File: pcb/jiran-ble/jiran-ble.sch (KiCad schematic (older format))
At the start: 166 parts, among them J1 BATT, J2 USB-C Conn, J3 SWD, J4 BATT, J5 USB-C Conn, J6 SWD, Q1 AO3407, Q3 AO3407, SW1 SW_PUSH, SW10 SW_Push, SW11 SW_Push, SW12 SW_Push, SW13 SW_Push, SW14 SW_Push, SW15 SW_Push, SW16 SW_Push, SW17 SW_Push, SW18 SW_Push, SW19 SW_Push, SW2 SW_Push, SW20 SW_Push, SW21 SW_Push, SW22 SW_Push, SW23 SW_Push, SW24 SW_Push, SW25 SW_Push, SW26 SW_Push, SW27 SW_Push, SW28 SW_Push, SW29 SW_Push, SW3 SW_Push, SW30 SW_PUSH, SW31 SW_Push, SW32 SW_Push, SW33 SW_Push, SW34 SW_Push, SW35 SW_Push, SW36 SW_Push, SW37 SW_Push, SW38 SW_Push, SW39 SW_Push, SW4 SW_Push, SW40 SW_Push, SW41 SW_Push, SW42 SW_Push, SW43 SW_Push, SW44 SW_Push, SW45 SW_Push, SW46 SW_Push, SW47 SW_Push, SW48 SW_Push, SW49 SW_Push, SW5 SW_Push, SW50 SW_Push, SW51 SW_Push, SW52 SW_Push, SW53 SW_Push, SW54 SW_Push, SW55 SW_Push, SW56 SW_Push, SW57 SW_Push, SW58 SW_Push, SW6 SW_Push, SW7 SW_Push, SW8 SW_Push, SW9 SW_Push, U1 XC6220B331MR-G, U2 E73-2G4M08S1C, U3 TP4054, U4 XC6220B331MR-G, U5 E73-2G4M08S1C, U6 TP4054, X1 Crystal, X2 Crystal

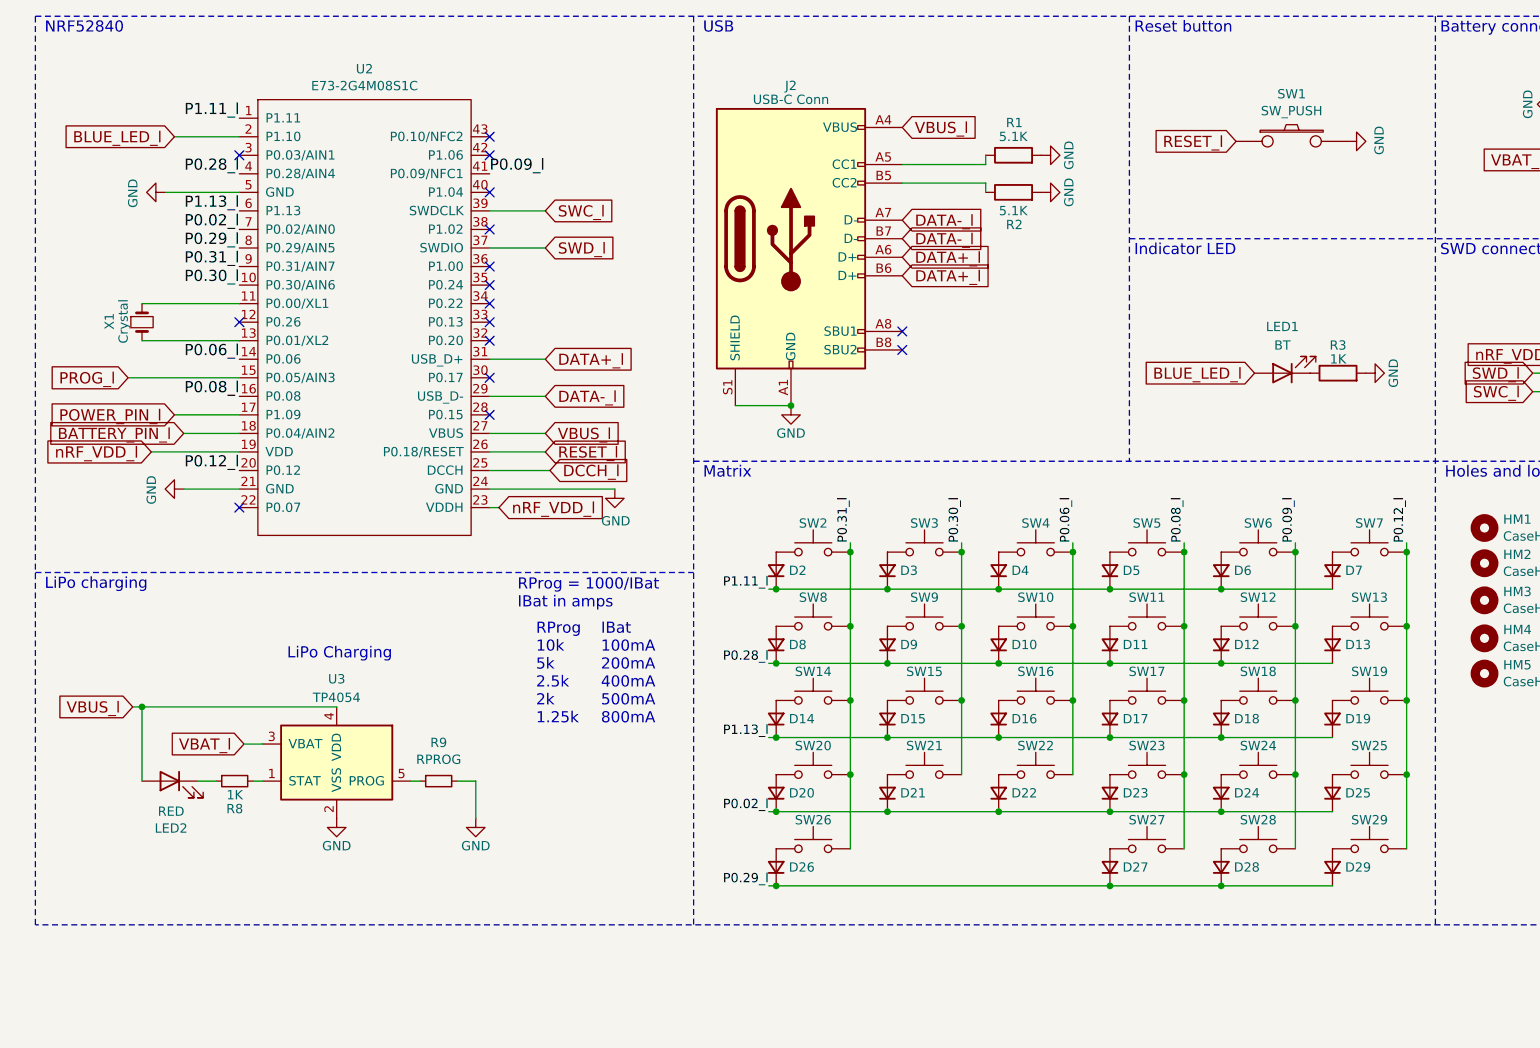
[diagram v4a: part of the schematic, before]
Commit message: Change controller module
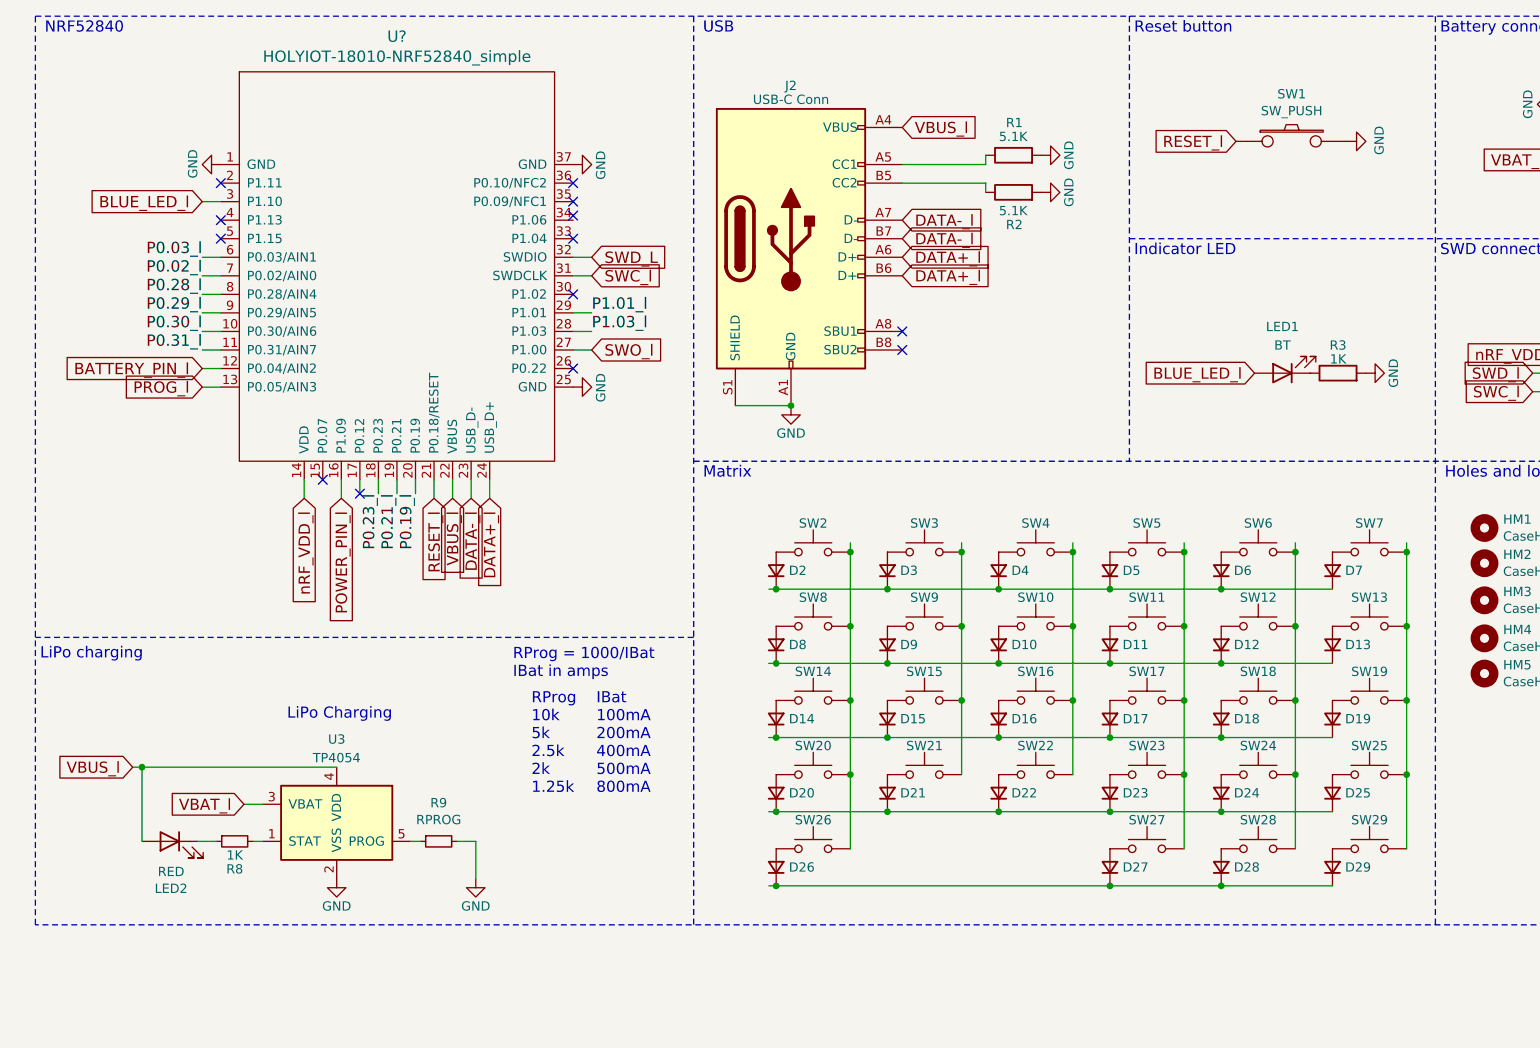
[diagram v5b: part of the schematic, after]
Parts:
- removed U2: E73-2G4M08S1C, jiran-ble:E73-2G4M08S1C-52840, symbol candy-rescue:E73-2G4M08S1C-52840-nrfmicro
- removed X1: Crystal, jiran-ble:Crystal_SMD_CM9V, symbol Device:Crystal_Small
- added U?: HOLYIOT-18010-NRF52840_simple, symbol jiran-ble:HOLYIOT-18010-NRF52840_simple
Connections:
- net labels added: P0.03_l, P0.19_l, P0.21_l, P0.23_l, P1.01_l, P1.03_l, SWD_L, SWO_l
- net labels removed: DCCH_l, P0.06_l, P0.08_l, P0.09_l, P0.12_l, P1.11_l, P1.13_l
- wire segments 227 -> 233
- no-connect marks 33 -> 30
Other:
- moved on the sheet: LED2, R8, R9, U3

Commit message: USB circuit is now simpler
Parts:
- removed R1, R2: 5.1K, jiran-ble:Resistor_SMD_0805, symbol Device:R
- added R? (x2): 5.1k, symbol Device:R_Small
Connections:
- net labels added: D+_l, D-_l
- wire segments 233 -> 245
- no-connect marks 30 -> 31
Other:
- note added: "USB-C"
- moved on the sheet: J2
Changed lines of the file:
@@
 NRF52840
 Text Notes 4100 600  0    60   ~ 0
-USB
+USB-C
 Text Notes 6425 1800 0    60   ~ 0
 Indicator LED
@@
 Text Notes 15415 11075 0    70   ~ 14
 r0.2
-Text GLabel 5175 1600 2    60   Input ~ 0
-DATA-_l
-$Comp
-L Device:R R2
-U 1 1 5CAA680B
-P 5775 1450
-F 0 "R2" V 5600 1400 50  0000 L CNN
-F 1 "5.1K" V 5675 1375 50  0000 L CNN
-F 2 "jiran-ble:Resistor_SMD_0805" V 5705 1450 50  0001 C CNN
-F 3 "~" H 5775 1450 50  0001 C CNN
-	1    5775 1450
-	0    -1   -1   0
-$EndComp
-$Comp
-L Device:R R1
-U 1 1 5CAA879F
-P 5775 1250
-F 0 "R1" V 5950 1200 50  0000 L CNN
-F 1 "5.1K" V 5875 1175 50  0000 L CNN
-F 2 "jiran-ble:Resistor_SMD_0805" V 5705 1250 50  0001 C CNN
-F 3 "~" H 5775 1250 50  0001 C CNN
-	1    5775 1250
-	0    -1   -1   0
-$EndComp
-Text GLabel 5175 1700 2    60   Input ~ 0
-DATA-_l
-Text GLabel 5175 1800 2    60   Input ~ 0
-DATA+_l
-Text GLabel 5175 1900 2    60   Input ~ 0
-DATA+_l
 $Comp
 L power:GND #PWR04
 U 1 1 5E5DBB46
-P 5925 1250
-F 0 "#PWR04" H 5925 1000 50  0001 C CNN
-F 1 "GND" H 5925 1100 50  0000 C CNN
-F 2 "" H 5925 1250 50  0001 C CNN
-F 3 "" H 5925 1250 50  0001 C CNN
-	1    5925 1250
-	0    -1   -1   0
-$EndComp
-$Comp
-L power:GND #PWR06
-U 1 1 5E5DDBCF
-P 5925 1450
-F 0 "#PWR06" H 5925 1200 50  0001 C CNN
-F 1 "GND" H 5925 1300 50  0000 C CNN
-F 2 "" H 5925 1450 50  0001 C CNN
-F 3 "" H 5925 1450 50  0001 C CNN
-	1    5925 1450
+P 6050 1300
+F 0 "#PWR04" H 6050 1050 50  0001 C CNN
+F 1 "GND" H 6050 1150 50  0000 C CNN
+F 2 "" H 6050 1300 50  0001 C CNN
+F 3 "" H 6050 1300 50  0001 C CNN
+	1    6050 1300
 	0    -1   -1   0
 $EndComp
@@
 L power:GND #PWR013
 U 1 1 5E5EC00A
-P 4575 2600
-F 0 "#PWR013" H 4575 2350 50  0001 C CNN
-F 1 "GND" H 4575 2450 50  0000 C CNN
-F 2 "" H 4575 2600 50  0001 C CNN
-F 3 "" H 4575 2600 50  0001 C CNN
-	1    4575 2600
+P 4650 2550
+F 0 "#PWR013" H 4650 2300 50  0001 C CNN
+F 1 "GND" H 4650 2400 50  0000 C CNN
+F 2 "" H 4650 2550 50  0001 C CNN
+F 3 "" H 4650 2550 50  0001 C CNN
+	1    4650 2550
 	1    0    0    -1
 $EndComp
-Text GLabel 5175 1100 2    60   Input ~ 0
+Text GLabel 5350 1050 2    60   Input ~ 0
 VBUS_l
 $Comp
 L nrfmicro-rescue:USB_C_Receptacle_USB2.0-Connector J2
 U 1 1 5C743564
-P 4575 1700
-F 0 "J2" H 4575 2525 50  0000 C CNN
-F 1 "USB-C Conn" H 4575 2450 50  0000 C CNN
-F 2 "jiran-ble:USB-C_MidMount" H 4682 2475 50  0001 C CNN
-F 3 "https://www.usb.org/sites/default/files/documents/usb_type-c.zip" H 4725 1700 50  0001 C CNN
-	1    4575 1700
+P 4650 1650
+F 0 "J2" H 4650 2475 50  0000 C CNN
+F 1 "USB-C Conn" H 4650 2400 50  0000 C CNN
+F 2 "jiran-ble:USB-C_MidMount" H 4757 2425 50  0001 C CNN
+F 3 "https://www.usb.org/sites/default/files/documents/usb_type-c.zip" H 4800 1650 50  0001 C CNN
+	1    4650 1650
 	1    0    0    -1
 $EndComp
@@
 Connection ~ 1075 4550
 Wire Wire Line
-	4275 2600 4575 2600
-Connection ~ 4575 2600
-Wire Wire Line
 	1675 4950 1725 4950
 Wire Wire Line
@@
 Wire Wire Line
 	11825 2050 11925 2050
-NoConn ~ 5175 2200
-NoConn ~ 5175 2300
+NoConn ~ 5250 2150
+NoConn ~ 5250 2250
 Text Notes 3175 4700 0    60   ~ 0
 RProg\n10k\n5k\n2.5k\n2k\n1.25k
@@
 Text Notes 3075 4075 0    60   ~ 0
 RProg = 1000/IBat\nIBat in amps
-Wire Wire Line
-	5175 1300 5625 1300
-Wire Wire Line
-	5625 1300 5625 1250
-Wire Wire Line
-	5175 1400 5625 1400
-Wire Wire Line
-	5625 1400 5625 1450
 Text GLabel 8775 2325 0    60   Input ~ 0
 nRF_VDD_l
@@
 NoConn ~ 3400 2000
 NoConn ~ 3400 1700
-NoConn ~ 3400 1575
+NoConn ~ 3400 1600
 NoConn ~ 3400 1500
 NoConn ~ 3400 1400
 NoConn ~ 1500 1600
 NoConn ~ 1500 1700
+$Comp
+L Device:R_Small R?
+U 1 1 609F1795
+P 5850 1250
+F 0 "R?" V 6025 1250 50  0000 C CNN
+F 1 "5.1k" V 5925 1250 50  0000 C CNN
+F 2 "" H 5850 1250 50  0001 C CNN
+F 3 "~" H 5850 1250 50  0001 C CNN
+	1    5850 1250
+	0    -1   -1   0
+$EndComp
+$Comp
+L Device:R_Small R?
+U 1 1 609F2B00
+P 5850 1350
+F 0 "R?" V 6025 1350 50  0000 C CNN
+F 1 "5.1k" V 5925 1350 50  0000 C CNN
+F 2 "" H 5850 1350 50  0001 C CNN
+F 3 "~" H 5850 1350 50  0001 C CNN
+	1    5850 1350
+	0    1    1    0
+$EndComp
+Text GLabel 5450 1600 2    61   Input ~ 0
+D-_l
+Wire Wire Line
+	5250 1550 5350 1550
+Wire Wire Line
+	5350 1650 5250 1650
+Wire Wire Line
+	5350 1550 5350 1600
+Wire Wire Line
+	5450 1600 5350 1600
+Connection ~ 5350 1600
+Wire Wire Line
+	5350 1600 5350 1650
+Text GLabel 5450 1800 2    61   Input ~ 0
+D+_l
+Wire Wire Line
+	5250 1750 5350 1750
+Wire Wire Line
+	5350 1850 5250 1850
+Wire Wire Line
+	5350 1750 5350 1800
+Wire Wire Line
+	5450 1800 5350 1800
+Connection ~ 5350 1800
+Wire Wire Line
+	5350 1800 5350 1850
+Wire Wire Line
+	5350 1050 5250 1050
+Wire Wire Line
+	5750 1350 5250 1350
+Wire Wire Line
+	5750 1250 5250 1250
+Wire Wire Line
+	5950 1250 6050 1250
+Wire Wire Line
+	6050 1350 5950 1350
+NoConn ~ 4350 2550
+Wire Wire Line
+	6050 1250 6050 1300
+Connection ~ 6050 1300
+Wire Wire Line
+	6050 1300 6050 1350
 $EndSCHEMATC

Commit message: Add bypass caps and change some resistor symbols
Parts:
- removed R3: 1K, jiran-ble:Resistor_SMD_0805, symbol Device:R
- added C?: 4.7uF, symbol Device:C_Small
- added R?: 1k, symbol Device:R_Small
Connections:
- wire segments 245 -> 251
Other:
- moved on the sheet: C?, D1, LED2, Q1, R4, R5, R7, R8, R9, SW?A, U1, U3
